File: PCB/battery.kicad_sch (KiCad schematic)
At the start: 1 part

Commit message: task: write matched LCSC part numbers into the schematic
Adds scripts/apply_lcsc_fields.py, which clones each symbol's existing
Manufacturer_Part_Number property (same indentation/effects) into a new
'LCSC' field with the matched code -- the field name the Fabrication
Toolkit plugin already installed in this repo recognizes for JLCPCB BOM
matching.

Applied the 31 confirmed matches from jlc_match.py across all sheets
(68 individual references). C_BUCK_OUT1 and R_ISET1 are left without an
LCSC field -- JLC doesn't stock those exact Yageo part numbers, to be
sorted out separately.

Verified: kicad-cli sch export bom round-trips every LCSC value
correctly, and ERC reports 0 violations.

Also switched jlc_match.py's BOM export to unranged references so each
match maps cleanly to individual schematic symbols.

Co-Authored-By: Claude Sonnet 5 <noreply@anthropic.com>
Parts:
- BT1: LCSC (none) -> C265016
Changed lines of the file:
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@@
+			)
+		)
+		(property "LCSC" "C265016"
+			(at 0 0 0)
+			(hide yes)
+			(show_name no)
+			(do_not_autoplace no)
+			(effects
+				(font
+					(size 1.27 1.27)
+				)
 			)
 		)

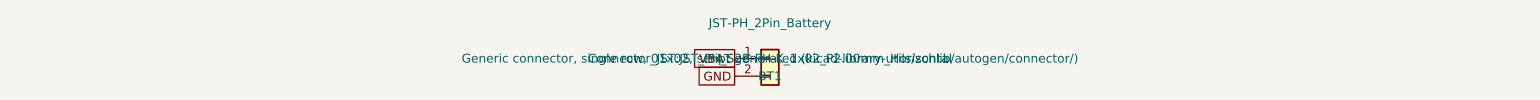
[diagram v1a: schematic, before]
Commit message: fix: power-latch false-trigger, RGB LED footprint regression, JST connector clarity (#56)
Power latch: battery-only bring-up showed the board powering on immediately
with no button press, because PWR_BTN_SENSE's resistor divider idled at
~VSYS/2, forward-biasing D_OR1's anode directly. Adds a transistor inverter
(R_INV_BASE1 / Q_INV1 / R_INV_PU1) so only an actual button press can
forward-bias D_OR1; removes the now-unnecessary R_PWR_SENSE1. New parts
matched to JLCPCB Basic-library equivalents. PCB layout, diagrams, and
power_control_layout docs updated to match.

RGB LED: fixes a regression where D_RGB1's Footprint had reverted to the
stale large SK6812 PLCC4 part in both the cached lib_symbols default and the
instance override, instead of the custom SK6812MINI-E-012 footprint that
PCBWay's earlier assembly rejection required.

JST battery connector: PCBWay's assembly mounted BT1 vertically instead of
horizontal. Confirmed via two independent distributor sources (JLC + LCSC)
that the specified MPN (S2B-PH-K(LF)(SN)) is genuinely a right-angle/
horizontal part, so this was an assembly-side error, not a design bug.
Made the Value/Description fields explicitly say RIGHT-ANGLE / HORIZONTAL
so it's unambiguous in the exported BOM this time.

Co-authored-by: Claude Sonnet 5 <noreply@anthropic.com>
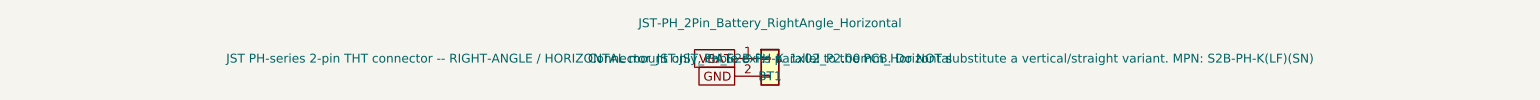
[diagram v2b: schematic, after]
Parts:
- BT1: value JST-PH_2Pin_Battery -> JST-PH_2Pin_Battery_RightAngle_Horizontal
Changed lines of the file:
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@@
 			)
 		)
-		(property "Value" "JST-PH_2Pin_Battery"
+		(property "Value" "JST-PH_2Pin_Battery_RightAngle_Horizontal"
 			(at 148.59 100.33 0)
 			(show_name no)
@@
 			)
 		)
-		(property "Description" "Generic connector, single row, 01x02, script generated (kicad-library-utils/schlib/autogen/connector/)"
+		(property "Description" "JST PH-series 2-pin THT connector -- RIGHT-ANGLE / HORIZONTAL mount only, cable exits parallel to the PCB. Do NOT substitute a vertical/straight variant. MPN: S2B-PH-K(LF)(SN)"
 			(at 148.59 105.41 0)
 			(show_name no)
